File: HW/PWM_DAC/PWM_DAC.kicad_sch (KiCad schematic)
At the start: 0 parts

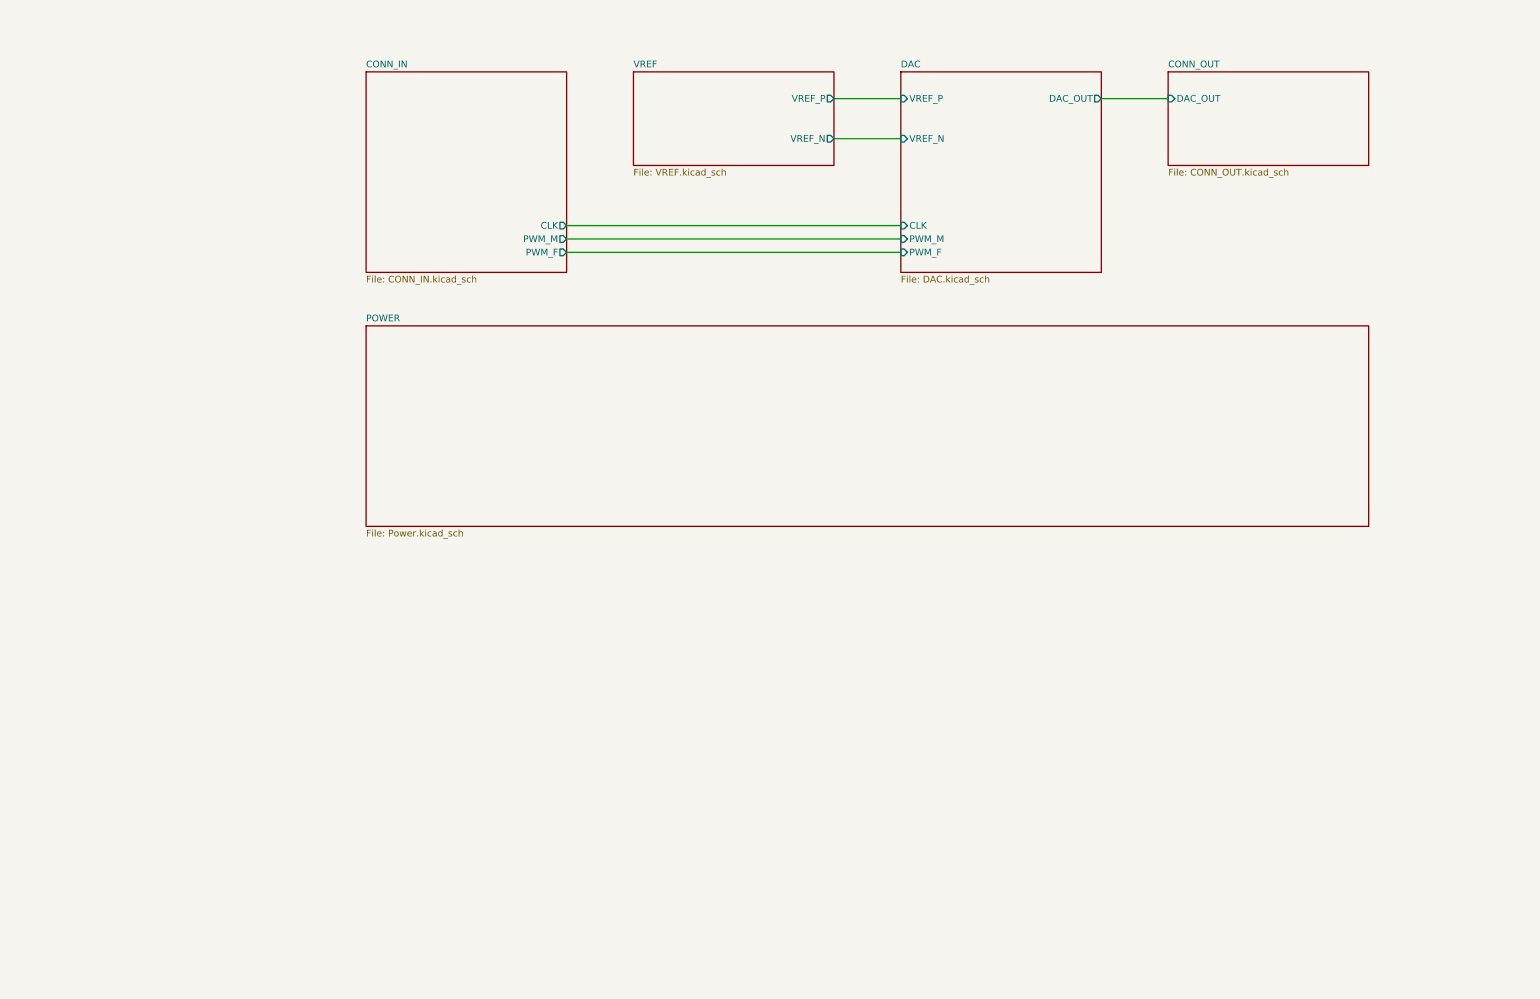
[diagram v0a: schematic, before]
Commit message: Schematic done
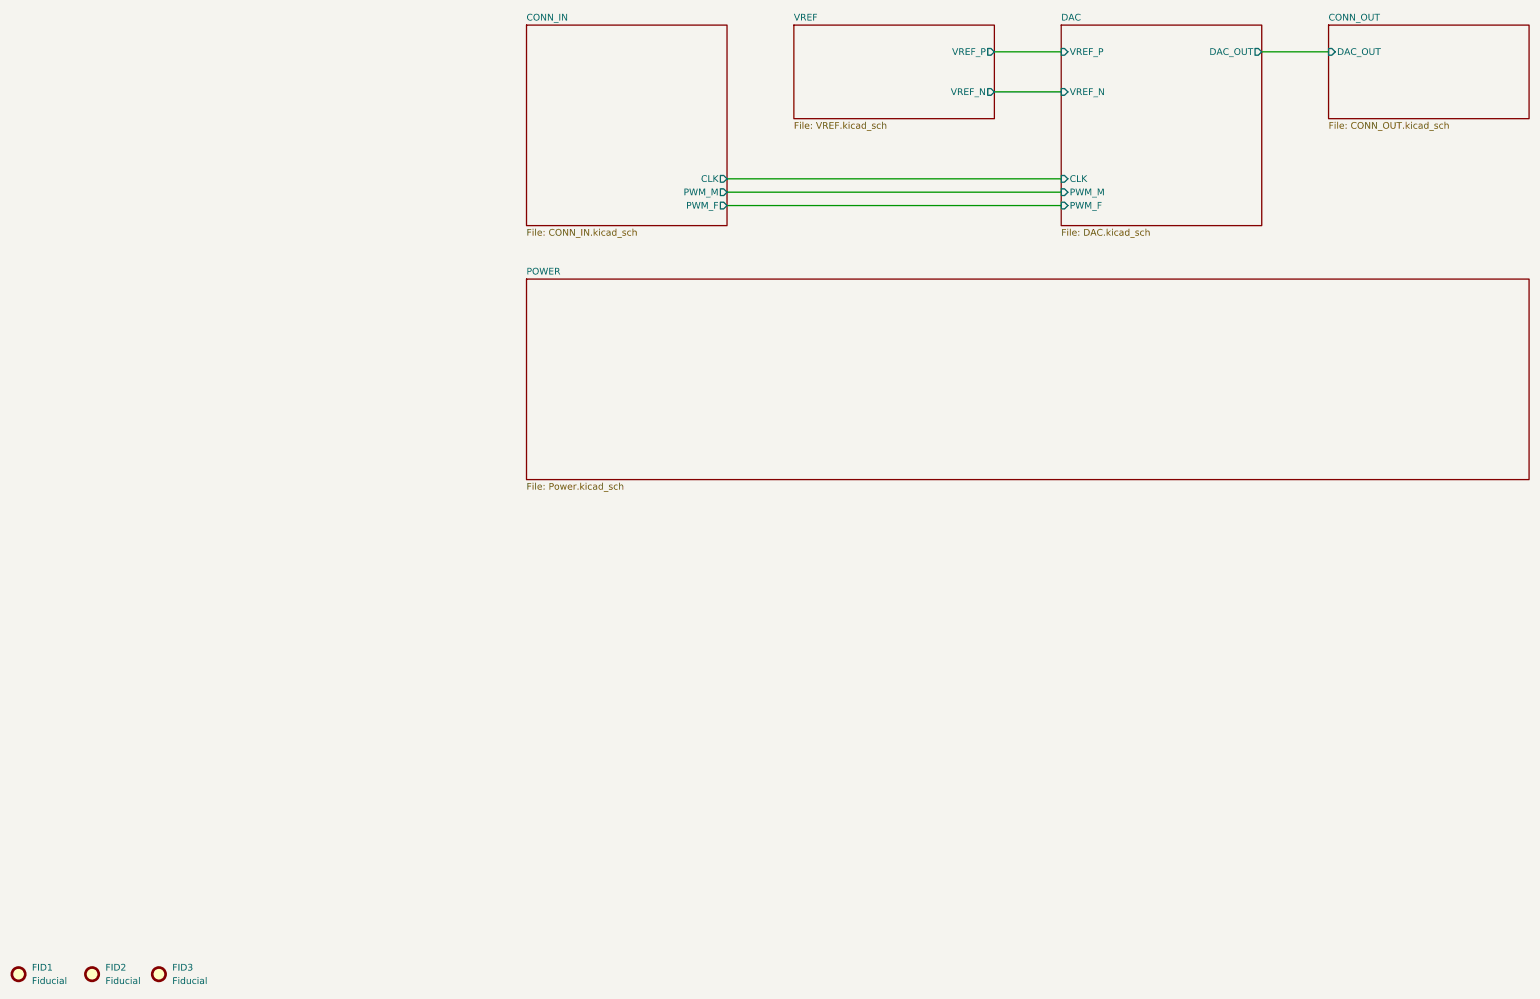
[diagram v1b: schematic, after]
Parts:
- added FID1, FID2, FID3: Fiducial, Fiducial:Fiducial_1.5mm_Mask3mm, symbol Mechanical:Fiducial
